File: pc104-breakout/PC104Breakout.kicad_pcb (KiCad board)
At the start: 2 copper layers, 165.1 x 56.5 mm, 109 parts, among them T1 Testpoint, T10 Testpoint, T100 Testpoint, T101 Testpoint, T102 Testpoint, T103 Testpoint, T104 Testpoint, T11 Testpoint, T12 Testpoint, T13 Testpoint, T14 Testpoint, T15 Testpoint, T16 Testpoint, T17 Testpoint, T18 Testpoint, T19 Testpoint, T2 Testpoint, T20 Testpoint, T21 Testpoint, T22 Testpoint, T23 Testpoint, T24 Testpoint, T25 Testpoint, T26 Testpoint, T27 Testpoint, T28 Testpoint, T29 Testpoint, T3 Testpoint, T30 Testpoint, T31 Testpoint, T32 Testpoint, T33 Testpoint, T34 Testpoint, T35 Testpoint, T36 Testpoint, T37 Testpoint, T38 Testpoint, T39 Testpoint, T4 Testpoint, T40 Testpoint, T41 Testpoint, T42 Testpoint, T43 Testpoint, T44 Testpoint, T45 Testpoint, T46 Testpoint, T47 Testpoint, T48 Testpoint, T49 Testpoint, T5 Testpoint, T50 Testpoint, T51 Testpoint, T52 Testpoint, T53 Testpoint, T54 Testpoint, T55 Testpoint, T56 Testpoint, T57 Testpoint, T58 Testpoint, T59 Testpoint, T6 Testpoint, T60 Testpoint, T61 Testpoint, T62 Testpoint, T63 Testpoint, T64 Testpoint, T65 Testpoint, T66 Testpoint, T67 Testpoint, T68 Testpoint, T69 Testpoint, T7 Testpoint, T70 Testpoint, T71 Testpoint, T72 Testpoint, T73 Testpoint, T74 Testpoint, T75 Testpoint, T76 Testpoint, T77 Testpoint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

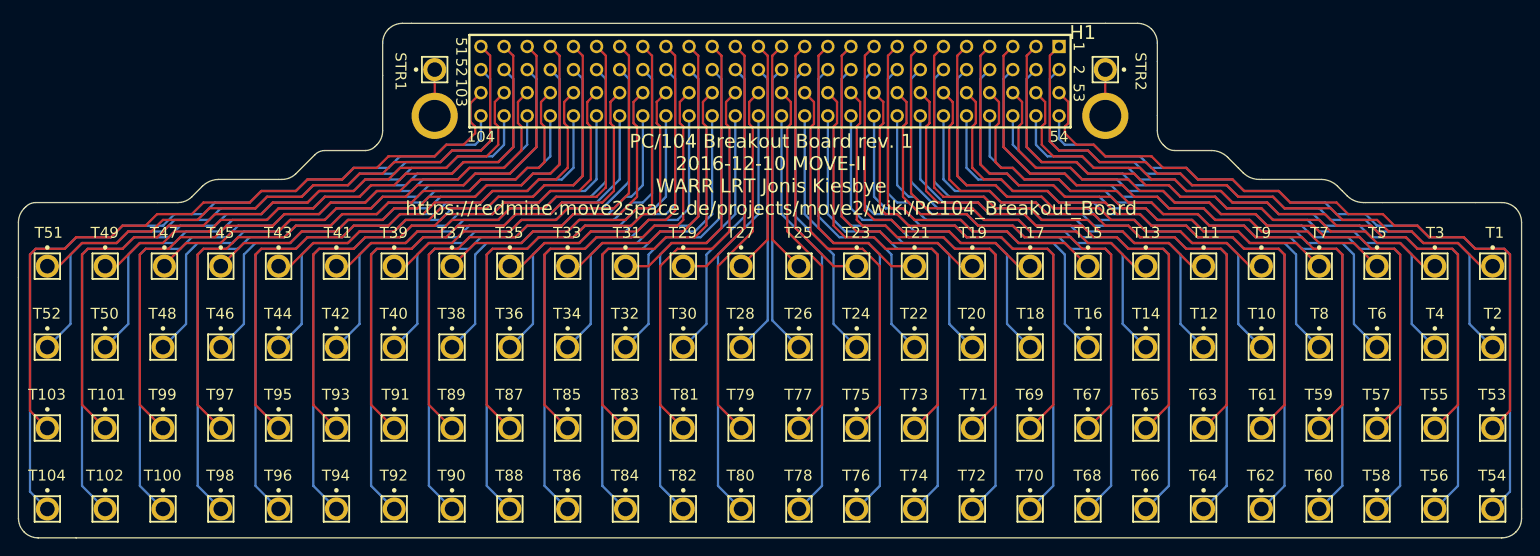
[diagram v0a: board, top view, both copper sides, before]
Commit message: adapt bridge and breakout to jlcpcb tolerance, add pin numbers to mainboard
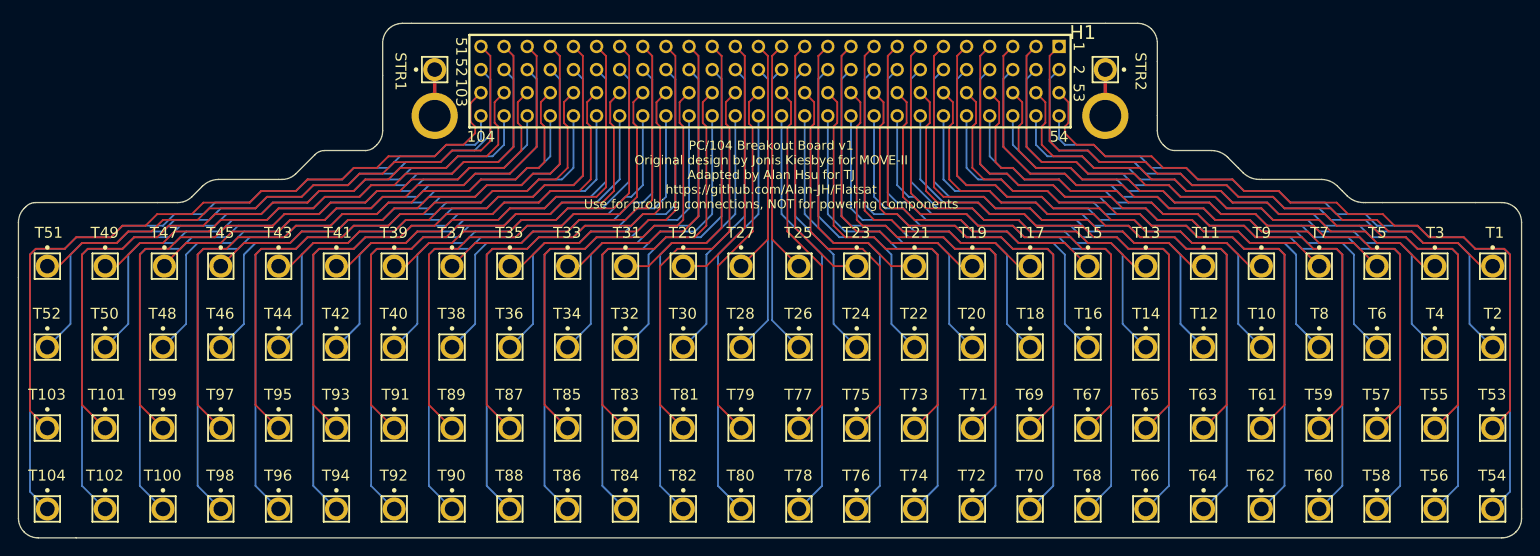
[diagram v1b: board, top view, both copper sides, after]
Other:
- board text added: "PC/104 Breakout Board v1 Original design by Jonis Kiesbye for MOVE-II Adapted by Alan Hsu for TJ https://github.com/Alan-JH/Flatsat Use for probing connections, NOT for powering components"
- board text removed: "PC/104 Breakout Board rev. 1 2016-12-10 MOVE-II WARR LRT Jonis Kiesbye https://redmine.move2space.de/projects/move2/wiki/PC104_Breakout_Board"
